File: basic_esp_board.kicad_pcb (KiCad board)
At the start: 2 copper layers, 78.7 x 44.4 mm, 31 parts, among them CON1 USB-MICRO-B, P1 CONN_SERIAL_SF, P2 HEADER_1, P3 HEADER_2, P4 HEADER_3, P6 WS2812, Q1 BSS138DW, SW1 SW_PUSH, U1 ESP-12E, U2 LD1117S33TR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

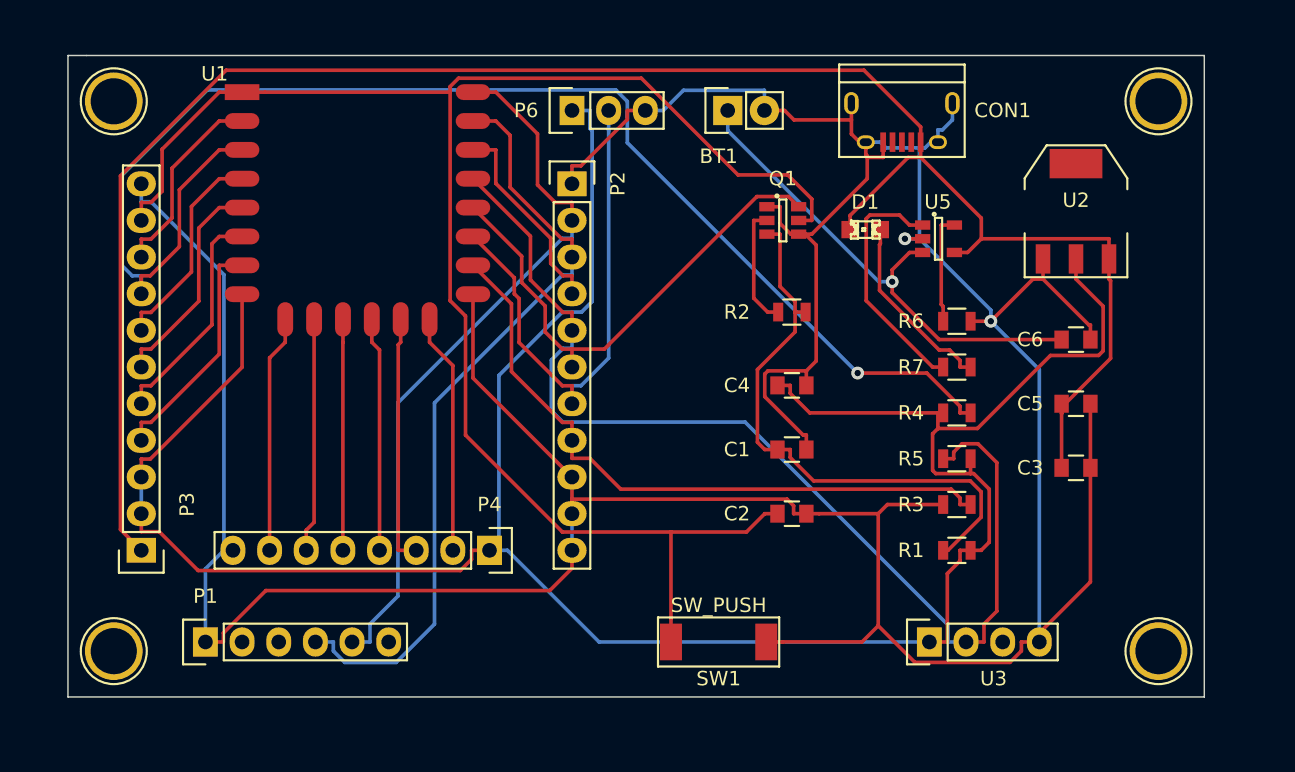
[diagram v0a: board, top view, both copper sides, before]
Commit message: Reroute board for new schematic, add ground plane
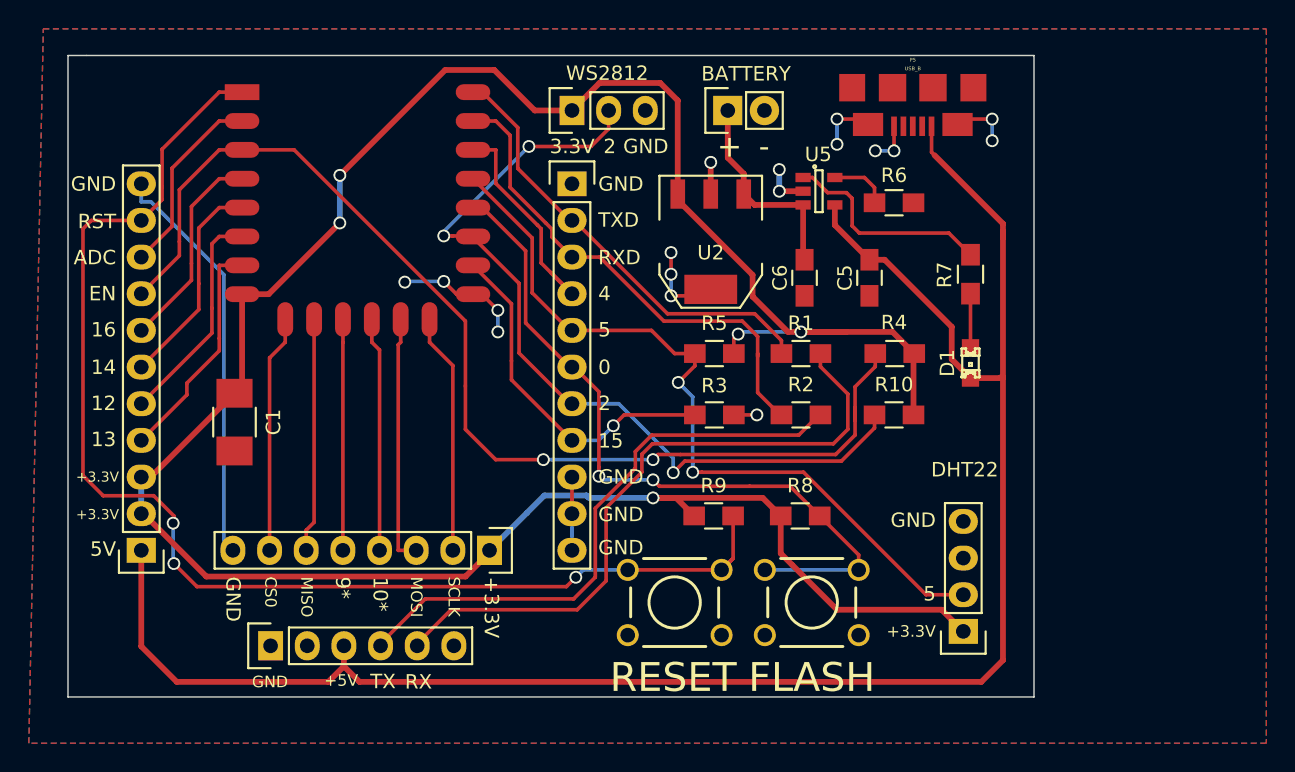
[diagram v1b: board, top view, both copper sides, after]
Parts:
- removed C2: 0.1u, Capacitors_SMD:C_0805
- removed C3: 100nF, Capacitors_SMD:C_0805
- removed C4: 10uF, Capacitors_SMD:C_0805
- removed CON1: USB-MICRO-B, Connect:USB_Micro-B
- removed Q1: BSS138DW, Housings_SOT-23_SOT-143_TSOT-6:SOT-23-6
- removed Z1, Z2, Z3, Z4: 1pin, Connect:1pin
- added P5: USB_B, molex_usb:USBMICROB_HIROSE_ZX62_B_5PA, F.Cu at (76.3, 25.2)
- added R10: 10K, Resistors_SMD:R_0805_HandSoldering, F.Cu at (75.0, 45.2)
- added R8: 10K, Resistors_SMD:R_0805_HandSoldering, F.Cu at (68.5, 52.2)
- added R9: 10K, Resistors_SMD:R_0805_HandSoldering, F.Cu at (62.5, 52.2)
- added SW2: RESET, FT:SW_PUSHBUTTON_PTH, F.Cu at (59.8, 58.2)
- C1: value 2u2 -> 100uF 6.3V X5R; footprint Capacitors_SMD:C_0805 -> Capacitors_SMD:C_1210_HandSoldering
- C5, C6: footprint Capacitors_SMD:C_0805 -> Capacitors_SMD:C_0805_HandSoldering
- R1: value 470K -> 4.7k; footprint Resistors_SMD:R_0805 -> Resistors_SMD:R_0805_HandSoldering
- R2: value 100K -> 4.7k; footprint Resistors_SMD:R_0805 -> Resistors_SMD:R_0805_HandSoldering
- R3, R4, R5, R6, R7: footprint Resistors_SMD:R_0805 -> Resistors_SMD:R_0805_HandSoldering
- SW1: value SW_PUSH -> PROG; footprint mage_mega:1107G -> FT:SW_PUSHBUTTON_PTH
- U2: value LD1117S33TR -> TC1262-33VDB
- U3: value AM2302 -> DHT22
- moved C1 38.7 mm to (29.3, 45.7), turned to 270 degrees
- moved U2 25.4 mm to (62.3, 33.2), turned to 180 degrees
- moved C6 19.3 mm to (68.8, 35.7), turned to 270 degrees
- moved R5 18.3 mm to (62.6, 41.0)
- moved R3 17.9 mm to (62.6, 45.2), turned to 180 degrees
- moved R1 17.4 mm to (68.6, 41.0)
- moved C5 16.8 mm to (73.3, 35.7), turned to 270 degrees
- moved D1 11.8 mm to (80.3, 41.6), turned to 90 degrees
- moved R6 9.29 mm to (75.0, 30.5)
- moved U5 8.92 mm to (69.8, 29.7)
- moved R2 7.15 mm to (68.6, 45.2)
- moved SW1 7.01 mm to (69.3, 58.2), turned to 180 degrees
- moved R7 6.50 mm to (80.3, 35.5), turned to 270 degrees
- moved R4 5.95 mm to (75.1, 41.0), turned to 180 degrees
- moved P1 4.52 mm to (31.8, 61.2)
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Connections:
- net Net-(P2-Pad4) renamed /GPIO4
- net Net-(P2-Pad5) renamed /GPIO5
- net Net-(P2-Pad7) renamed /GPIO2
- net Net-(P2-Pad8) renamed /GPIO15
- net Net-(P3-Pad4) renamed /GPIO13
- net Net-(P3-Pad5) renamed /GPIO12
- net Net-(P3-Pad6) renamed /GPIO14
- net Net-(P3-Pad7) renamed /GPIO16
- net Net-(P3-Pad8) renamed /EN
- net Net-(P3-Pad9) renamed /ADC
- net Net-(P4-Pad2) renamed /SCLK
- net Net-(P4-Pad3) renamed /MOSI
- net Net-(P4-Pad4) renamed /GPIO10
- net Net-(P4-Pad5) renamed /GPIO9
- net Net-(P4-Pad6) renamed /MISO
- net Net-(P4-Pad7) renamed /CS0
- BT1 pad 1: Net-(BT1-Pad1) -> +BATT
- C1 pad 1: Net-(C1-Pad1) -> +3V3
- C6 pad 1: Net-(BT1-Pad1) -> +BATT
- P1 pad 2: Net-(P1-Pad2) -> (no net)
- P1 pad 3: Net-(P1-Pad3) -> +5V
- P1 pad 6: Net-(P1-Pad6) -> (no net)
- P2 pad 2: Net-(P1-Pad5) -> /TXD
- P2 pad 3: Net-(P1-Pad4) -> /RXD
- R1 pad 1: Net-(C1-Pad1) -> /TXD
- R1 pad 2: +3V3 -> Net-(P1-Pad5)
- R2 pad 1: Net-(Q1-Pad2) -> /RXD
- R2 pad 2: Net-(C1-Pad1) -> Net-(P1-Pad4)
- SW1 pad 2: /RESET -> /GPIO0
- U1 pad 21: Net-(P1-Pad4) -> /RXD
- U1 pad 22: Net-(P1-Pad5) -> /TXD
- U2 pad 1: GND -> +BATT
- U2 pad 2: +3V3 -> GND
- U2 pad 3: +5V -> +3V3
- U3 pad 3: Net-(U3-Pad3) -> (no net)
- U5 pad 3: Net-(BT1-Pad1) -> +BATT
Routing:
- net GND: track 285.0 -> 66.7 mm, vias 2 -> 17
- net Net-(C1-Pad1): track 40.2 -> 0.00 mm
- net /RXD: track 0.00 -> 34.7 mm
- net Net-(BT1-Pad1): track 34.4 -> 0.00 mm, vias 1 -> 0
- net /TXD: track 0.00 -> 31.3 mm
- net /RESET: track 115.8 -> 90.6 mm, vias 0 -> 3
- net /GPIO2: track 36.6 -> 58.3 mm, vias 0 -> 3
- net /GPIO15: track 45.8 -> 24.2 mm, vias 0 -> 1
- net /GPIO5: track 75.3 -> 54.2 mm, vias 0 -> 2
- net /EN: track 95.8 -> 77.4 mm, vias 1 -> 2
- net /GPIO0: track 34.7 -> 50.6 mm, vias 0 -> 2
- net +BATT: track 0.00 -> 14.5 mm
- net Net-(P1-Pad4): track 53.7 -> 40.7 mm
- net +3V3: track 171.2 -> 182.2 mm, vias 0 -> 5
- net Net-(D1-Pad2): track 13.0 -> 3.75 mm
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- added copper zone on B.Cu, net GND
- added copper zone on F.Cu, net GND
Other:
- board size 78.7 x 44.4 mm -> 66.9 x 44.4 mm
- net class Default: clearance 0.254 -> 0.2
- net class Power added: clearance 0.2, trace_width 0.4, via_dia 0.889, via_drill 0.635
- rule trace_clearance: 0.254 -> 0.2
- board text added: "+"
- board text added: "+3.3V"
- board text added: "+5V"
- board text added: "-"
- board text added: "0"
- board text added: "10*"
- board text added: "12"
- board text added: "13"
- board text added: "14"
- board text added: "15"
- board text added: "16"
- board text added: "2"
- board text added: "3.3V"
- board text added: "4"
- board text added: "5"
- board text added: "5V"
- board text added: "9*"
- board text added: "ADC"
- board text added: "CS0"
- board text added: "EN"
- board text added: "FLASH"
- board text added: "GND"
- board text added: "MISO"
- board text added: "MOSI"
- board text added: "Project: basic_esp_board Designer: Mark Wolfe Email: mark@wolfe.id.au Website: www.wolfe.id.au Rev: 1.1"
- board text added: "RESET"
- board text added: "RST"
- board text added: "RX"
- board text added: "RXD"
- board text added: "SCLK"
- board text added: "TX"
- board text added: "TXD"
- board text removed: "Project: basic_esp_board Designer: Mark Wolfe Email: mark@wolfe.id.au Website: http://www.wolfe.id.au Rev: 1.0"
